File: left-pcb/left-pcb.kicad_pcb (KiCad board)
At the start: 2 copper layers, 124.8 x 104.5 mm, 43 parts, among them J1 BAT, U1 xiao-ble

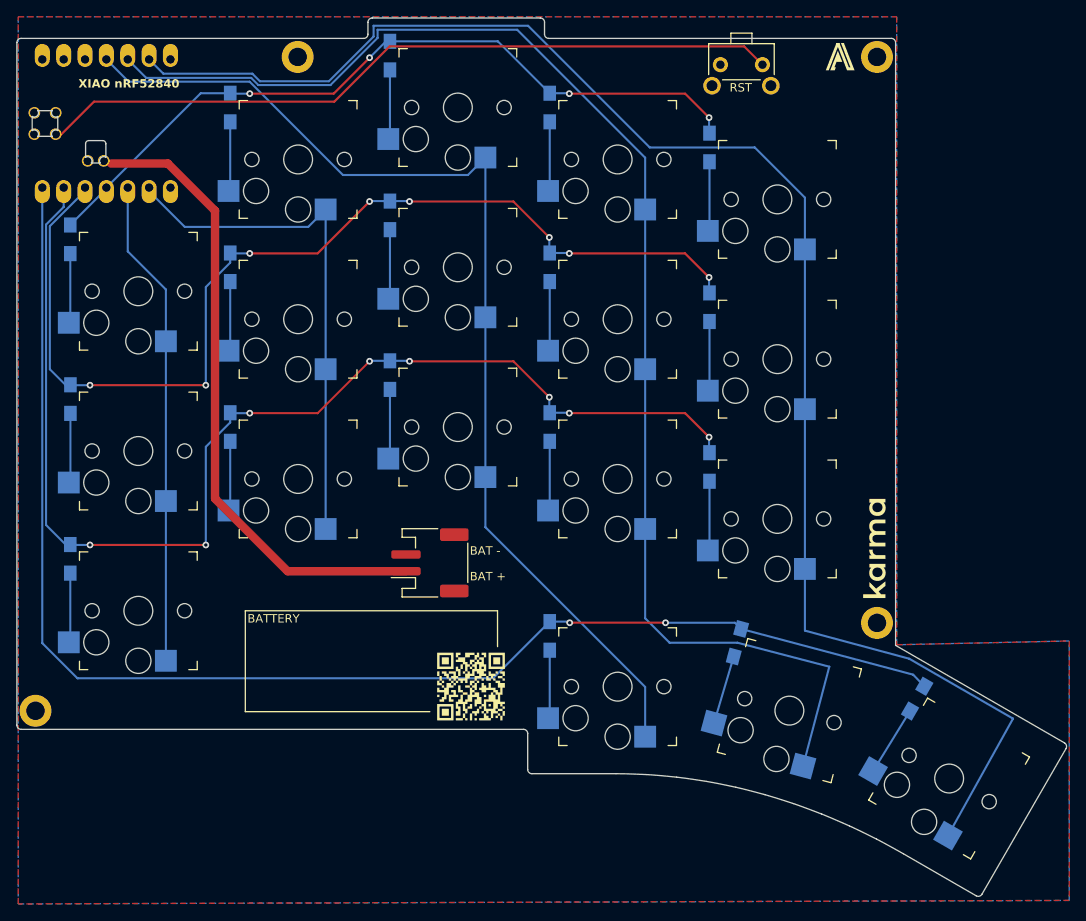
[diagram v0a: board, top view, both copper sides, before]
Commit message: Align mounting holes in left-pcb
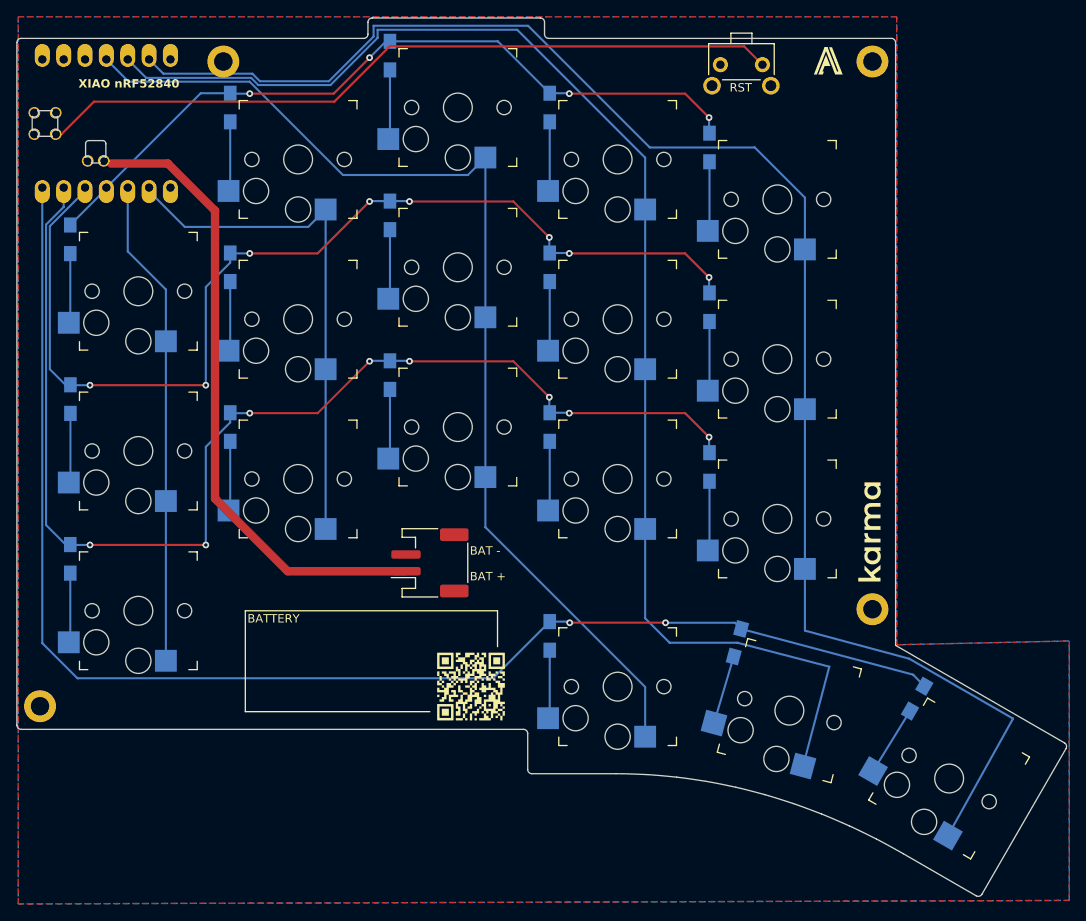
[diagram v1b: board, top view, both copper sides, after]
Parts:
- moved REF** 8.86 mm to (62.1, 38.5)
- moved REF** 1.72 mm to (139.3, 103.6)
- moved REF** 0.77 mm to (139.3, 38.5)
- moved REF** 0.76 mm to (40.3, 115.1)

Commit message: Fix DRC issues in left-pcb
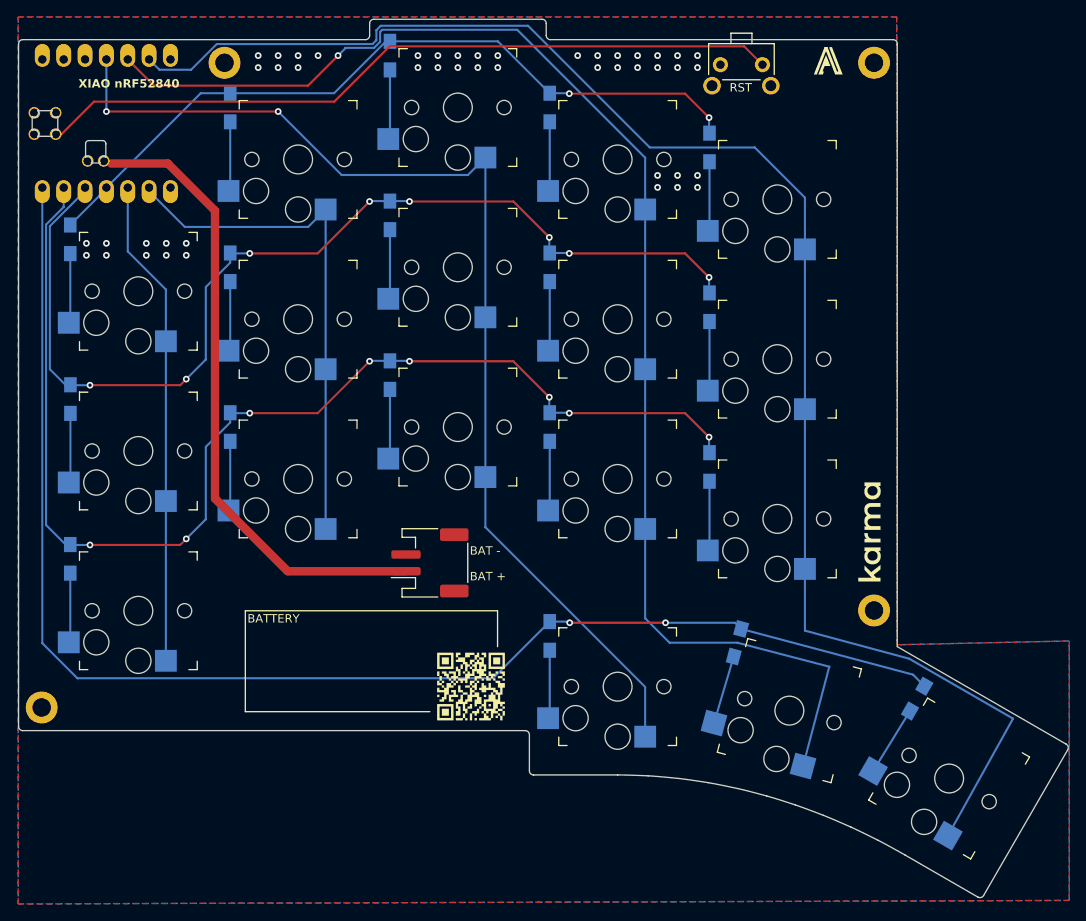
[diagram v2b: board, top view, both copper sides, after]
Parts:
- moved REF** 0.25 mm to (40.5, 115.3)
- moved REF** 0.24 mm to (139.5, 103.7)
- moved REF** 0.24 mm to (139.5, 38.6)
- moved REF** 0.21 mm to (62.3, 38.6)
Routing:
- net COL2_L: track 128.4 -> 132.0 mm, vias 0 -> 2
- net ROW2_L: track 144.1 -> 142.4 mm
- net ROW1_L: track 125.8 -> 124.0 mm
- net COL4_L: track 185.5 -> 184.3 mm
- net COL3_L: track 162.9 -> 163.1 mm, vias 0 -> 1
- net ROW0_L: track 90.8 -> 90.7 mm, vias 4 -> 2
- net GND_L: vias 0 -> 46
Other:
- outline, holes or cut-outs redrawn
